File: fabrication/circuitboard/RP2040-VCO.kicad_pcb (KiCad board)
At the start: 2 copper layers, 29 x 60 mm, 41 parts, among them J2 Power Input, J6 Conn_01x06_Male, J7 Conn_01x08_Male, U1 TL074, U2 Seed_XIAO_RP2040, U3 AP2210K-5.0TRG1

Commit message: update to v1.1
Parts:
- removed J6: Conn_01x06_Male, Connector_PinHeader_2.54mm:PinHeader_1x06_P2.54mm_Horizontal
- removed J7: Conn_01x08_Male, Connector_PinHeader_2.54mm:PinHeader_1x08_P2.54mm_Horizontal
- added H2: SpacerHoles, MountingHole:MountingHole_3.2mm_M3, F.Cu at (68.0, 96.0)
- added J1: Conn_01x06_Male, Connector_PinHeader_2.54mm:PinHeader_1x06_P2.54mm_Vertical, F.Cu at (69.7, 49.5)
- added J2: Conn_01x08_Male, Connector_PinHeader_2.54mm:PinHeader_1x08_P2.54mm_Vertical, F.Cu at (53.3, 67.8)
- D1: renamed from D3; footprint Diode_SMD:D_SOD-123 -> Kicad-perso:D_SOD-123
- D2: renamed from D4; footprint Diode_SMD:D_SOD-123 -> Kicad-perso:D_SOD-123
- D3: renamed from D1; footprint Diode_SMD:D_SOD-123 -> Kicad-perso:D_SOD-123
- D4: renamed from D2; footprint Diode_SMD:D_SOD-123 -> Kicad-perso:D_SOD-123
- J8: renamed from J2; moved to B.Cu
- U1: footprint Package_SO:SOIC-14_3.9x8.7mm_P1.27mm -> Kicad-perso:SOIC-14_3.9x8.7mm_P1.27mm
- U3: renamed from U2; moved to B.Cu
- moved C10 43.4 mm to (56.9, 118.1), turned to 0 degrees
- moved C9 40.8 mm to (56.9, 115.6), turned to 0 degrees
- moved J8 40.6 mm to (60.3, 140.9), turned to 0 degrees
- moved C7 38.2 mm to (56.9, 113.0), turned to 0 degrees
- moved C14 36.2 mm to (54.0, 127.3)
- moved C13 36.0 mm to (64.4, 124.8)
- moved C12 36.0 mm to (58.6, 124.8)
- moved C16 36.0 mm to (61.4, 128.2)
- moved U2 36.0 mm to (61.5, 125.0)
- moved C6 36.0 mm to (57.0, 110.5), turned to 0 degrees
- moved C15 35.7 mm to (69.0, 127.2)
- moved C11 35.4 mm to (66.1, 118.1), turned to 180 degrees
- moved U3 32.7 mm to (61.5, 110.5), turned to 0 degrees
- moved C8 31.7 mm to (66.1, 113.0), turned to 180 degrees
- moved C5 29.3 mm to (66.1, 107.5), turned to 0 degrees
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- renumbered C16 to C1, C5 to C10, C8 to C11, C11 to C13, C3 to C14, C4 to C15, C9 to C16, C7 to C2, C6 to C3, C14 to C4, C13 to C5, C2 to C6, C15 to C7, C10 to C8, C1 to C9, R5 to R1, R4 to R10, R6 to R11, R14 to R12, R3 to R13, R12 to R14, R10 to R15, R1 to R2, R2 to R3, R13 to R4, R16 to R5, R11 to R6, R15 to R7, R7 to R8, R8 to R9, U3 to U2
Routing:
- net +3V3: track 50.3 -> 101.6 mm, vias 2 -> 0
- net /Chord: track 21.6 -> 61.2 mm, vias 0 -> 1
- net /Tune: track 31.9 -> 68.4 mm, vias 0 -> 1
- net /SW_1: track 10.3 -> 45.7 mm, vias 0 -> 2
- net /Inv: track 33.3 -> 66.9 mm, vias 0 -> 3
- net +12V: track 110.7 -> 86.3 mm, vias 1 -> 2
- net Net-(C1-Pad2): track 23.2 -> 2.90 mm
- net -12V: track 66.8 -> 84.5 mm, vias 1 -> 2
- net +5V: track 58.2 -> 74.6 mm, vias 1 -> 0
- net /SW_0: track 13.7 -> 26.2 mm
- net /Push_SW: track 17.7 -> 28.7 mm
- net GND: track 3.90 -> 14.7 mm, vias 58 -> 42
- net Net-(U1B-+): track 11.9 -> 22.2 mm
- net /InvJack: track 30.7 -> 20.8 mm, vias 2 -> 0
- net /V/oct: track 44.7 -> 49.8 mm
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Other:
- board size 29 x 60 mm -> 20 x 110 mm
- board text added: "RP2040 VCO V1.1 BleepSound 2023"
- board text removed: "RP2040 VCO V1.0 BleepSound 2023"

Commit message: update silkscreen
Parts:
- renumbered C14 to C10, C3 to C11, C16 to C13, C13 to C14, C2 to C16, C5 to C2, C4 to C3, C9 to C4, C11 to C5, C8 to C6, C6 to C7, C10 to C8, C7 to C9, D3 to D1, D4 to D2, D1 to D3, D2 to D4, H2 to H1, J1 to J3, J2 to J5, R7 to R1, R11 to R10, R10 to R11, R8 to R12, R6 to R13, R9 to R14, R4 to R15, R12 to R16, R15 to R2, R14 to R3, R5 to R4, R2 to R5, R3 to R6, R1 to R8, R13 to R9, U3 to U2, U2 to U3
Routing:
- net GND: vias 42 -> 43

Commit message: update fab files and repo organization
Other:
- board text added: "RP2040 VCO V1.2 BleepSound 2023"
- board text removed: "RP2040 VCO V1.1 BleepSound 2023"
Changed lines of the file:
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@@
     (pad "5" smd rect (at 1.25 -0.95 180) (size 0.6 1.2) (layers "F.Cu" "F.Paste" "F.Mask")
       (net 7 "+5V") (pinfunction "VOUT") (pintype "power_in"))
-    (model "${KIPRJMOD}/3D/AP2210K-5.0TRG1.stp"
+    (model "${LIB_PERSO_3D}/AP2210K-5.0TRG1.stp"
       (offset (xyz 0 0 0))
       (scale (xyz 1 1 1))
@@
     (fp_rect (start -9.144 10.668) (end 9.144 -10.668)
       (stroke (width 0.12) (type solid)) (fill none) (layer "B.SilkS"))
-    (fp_rect (start -5.08 11.004) (end 5.08 4.4)
-      (stroke (width 0.12) (type solid)) (fill none) (layer "B.SilkS"))
+    (fp_rect (start -5.08 11.004) (end 5.08 9.2)
+      (stroke (width 0.12) (type solid)) (fill solid) (layer "B.SilkS"))
     (fp_rect (start -9.652 11.176) (end 9.652 -11.176)
       (stroke (width 0.05) (type solid)) (fill none) (layer "B.CrtYd"))
@@
     (pad "14" thru_hole circle (at 7.62 7.62) (size 1.7 1.7) (drill 1) (layers "*.Cu" "*.Mask")
       (net 7 "+5V") (pinfunction "5V") (pintype "power_in"))
-    (model "${KIPRJMOD}/3D/Seeed Studio XIAO RP2040 v26.step"
+    (model "${LIB_PERSO_3D}/Seeed Studio XIAO RP2040 v26.step"
       (offset (xyz 0 0 5))
       (scale (xyz 1 1 1))
@@
     (effects (font (size 1.5 1.5) (thickness 0.3)) (justify mirror))
   )
-  (gr_text "RP2040 VCO\nV1.1 BleepSound\n2023" (at 61.6 40.7) (layer "F.SilkS")
+  (gr_text "RP2040 VCO\nV1.2 BleepSound\n2023" (at 61.6 40.7) (layer "F.SilkS")
     (effects (font (size 1 1) (thickness 0.15)))
   )
@@
   (via (at 56.2 93.2) (size 0.8) (drill 0.4) (layers "F.Cu" "B.Cu") (free) (net 1))
   (via (at 64.6 89.7) (size 0.8) (drill 0.4) (layers "F.Cu" "B.Cu") (free) (net 1))
-  (via (at 69.7 88) (size 0.8) (drill 0.4) (layers "F.Cu" "B.Cu") (free) (net 1))
+  (via (at 69.3 88) (size 0.8) (drill 0.4) (layers "F.Cu" "B.Cu") (free) (net 1))
   (via (at 55.9 50.2) (size 0.8) (drill 0.4) (layers "F.Cu" "B.Cu") (free) (net 1))
-  (via (at 69.7 87.1) (size 0.8) (drill 0.4) (layers "F.Cu" "B.Cu") (free) (net 1))
+  (via (at 69.3 87.1) (size 0.8) (drill 0.4) (layers "F.Cu" "B.Cu") (free) (net 1))
   (via (at 64.2 68.5) (size 0.8) (drill 0.4) (layers "F.Cu" "B.Cu") (free) (net 1))
   (via (at 53.6 91.2) (size 0.8) (drill 0.4) (layers "F.Cu" "B.Cu") (free) (net 1))
   (via (at 59.7 120.7) (size 0.8) (drill 0.4) (layers "F.Cu" "B.Cu") (free) (net 1))
   (via (at 66.1 85.4) (size 0.8) (drill 0.4) (layers "F.Cu" "B.Cu") (free) (net 1))
-  (via (at 69.7 88.9) (size 0.8) (drill 0.4) (layers "F.Cu" "B.Cu") (free) (net 1))
+  (via (at 69.3 88.9) (size 0.8) (drill 0.4) (layers "F.Cu" "B.Cu") (free) (net 1))
   (via (at 66.1 86.3) (size 0.8) (drill 0.4) (layers "F.Cu" "B.Cu") (free) (net 1))
   (via (at 59.8 84) (size 0.8) (drill 0.4) (layers "F.Cu" "B.Cu") (free) (net 1))
@@
   (segment (start 69.12 118.12) (end 67.1575 118.12) (width 0.3) (layer "F.Cu") (net 7))
   (segment (start 58.6 123.8125) (end 60.5375 123.8125) (width 0.3) (layer "F.Cu") (net 7))
+  (segment (start 70.3 100.002943) (end 70.3 79.660661) (width 0.3) (layer "B.Cu") (net 7))
+  (segment (start 68.25 77.610661) (end 68.25 61.11) (width 0.3) (layer "B.Cu") (net 7))
+  (segment (start 68.25 61.11) (end 69.7 59.66) (width 0.3) (layer "B.Cu") (net 7))
   (segment (start 67.92 116.92) (end 67.92 102.382943) (width 0.3) (layer "B.Cu") (net 7))
-  (segment (start 68.25 77.610661) (end 68.25 61.11) (width 0.3) (layer "B.Cu") (net 7))
+  (segment (start 70.3 79.660661) (end 68.25 77.610661) (width 0.3) (layer "B.Cu") (net 7))
   (segment (start 69.12 118.12) (end 67.92 116.92) (width 0.3) (layer "B.Cu") (net 7))
-  (segment (start 67.92 102.382943) (end 70.7 99.602943) (width 0.3) (layer "B.Cu") (net 7))
-  (segment (start 70.7 80.060661) (end 68.25 77.610661) (width 0.3) (layer "B.Cu") (net 7))
-  (segment (start 68.25 61.11) (end 69.7 59.66) (width 0.3) (layer "B.Cu") (net 7))
-  (segment (start 70.7 99.602943) (end 70.7 80.060661) (width 0.3) (layer "B.Cu") (net 7))
+  (segment (start 67.92 102.382943) (end 70.3 100.002943) (width 0.3) (layer "B.Cu") (net 7))
   (segment (start 59.85 86.9) (end 58.8 85.85) (width 0.3) (layer "F.Cu") (net 8))
   (segment (start 61.75 78.35) (end 65.7 78.35) (width 0.3) (layer "F.Cu") (net 8))
@@
   (segment (start 67.1775 113.04) (end 67.1375 113) (width 0.3) (layer "F.Cu") (net 8))
   (segment (start 57.8 94.7) (end 57.8 103.6625) (width 0.3) (layer "F.Cu") (net 8))
-  (segment (start 71.2 110.96) (end 69.12 113.04) (width 0.3) (layer "B.Cu") (net 8))
-  (segment (start 71.2 63.7) (end 71.2 110.96) (width 0.3) (layer "B.Cu") (net 8))
-  (segment (start 69.7 62.2) (end 71.2 63.7) (width 0.3) (layer "B.Cu") (net 8))
+  (segment (start 70.8 111.36) (end 70.8 63.3) (width 0.3) (layer "B.Cu") (net 8))
+  (segment (start 69.12 113.04) (end 70.8 111.36) (width 0.3) (layer "B.Cu") (net 8))
+  (segment (start 70.8 63.3) (end 69.7 62.2) (width 0.3) (layer "B.Cu") (net 8))
   (segment (start 63.35 79.3) (end 64.25 79.3) (width 0.3) (layer "F.Cu") (net 9))
   (segment (start 70 65.6) (end 70 64.1) (width 0.3) (layer "F.Cu") (net 9))

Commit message: V1.4 update
add extra 10k resistor on inv CV input (missing)
Update BoM for clarity
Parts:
- added R18: 10k, Resistor_SMD:R_0805_2012Metric_Pad1.20x1.40mm_HandSolder, F.Cu at (61.5, 77.5)
- moved D3 0.40 mm to (65.0, 79.7)
- moved D4 0.40 mm to (65.0, 82.1)
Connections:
- R10 pad 2: /InvJack -> Net-(U1C--)
- R12 pad 1: /InvJack -> Net-(U1C--)
- U1 pad 9: /InvJack -> Net-(U1C--)
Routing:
- net /InvJack: track 20.8 -> 11.6 mm
- net Net-(U1C--): track 0.00 -> 9.18 mm
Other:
- board text added: "RP2040 VCO V1.4 BleepSound 2025"
- board text removed: "RP2040 VCO V1.2 BleepSound 2023"

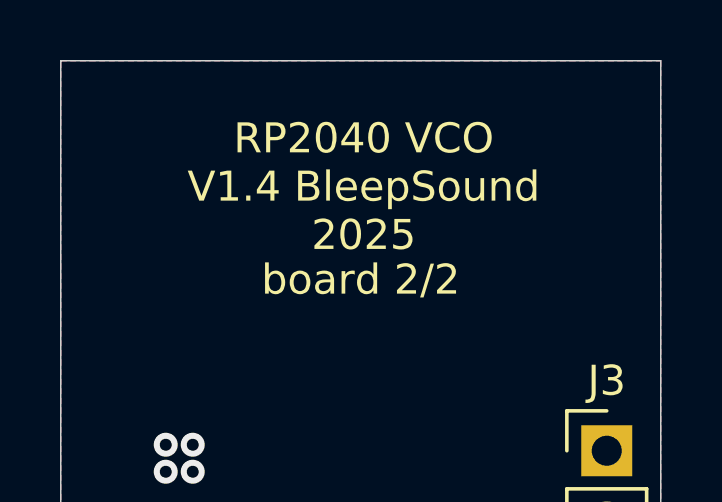
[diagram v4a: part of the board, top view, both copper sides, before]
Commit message: v1.5
reverse pots following issue raised on github
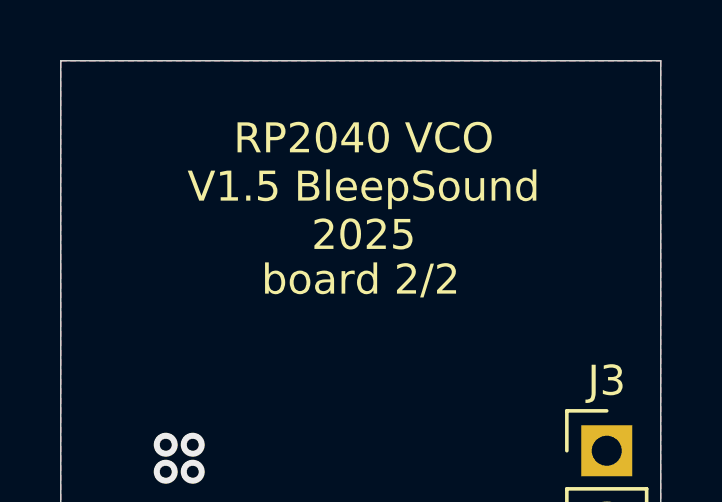
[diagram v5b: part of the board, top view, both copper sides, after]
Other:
- board text added: "RP2040 VCO V1.5 BleepSound 2025"
- board text removed: "RP2040 VCO V1.4 BleepSound 2025"
